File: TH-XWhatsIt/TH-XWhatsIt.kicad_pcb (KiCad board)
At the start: 2 copper layers, 162.2 x 18.8 mm, 25 parts, among them J1 BEAMSPRING CONNECTOR, J3 EXPANSION HEADER, U1 MCP4921-EP, U2 LM339, U3 74HCT595, U4 74HCT595, U5 ProMicro, U7 74HCT595

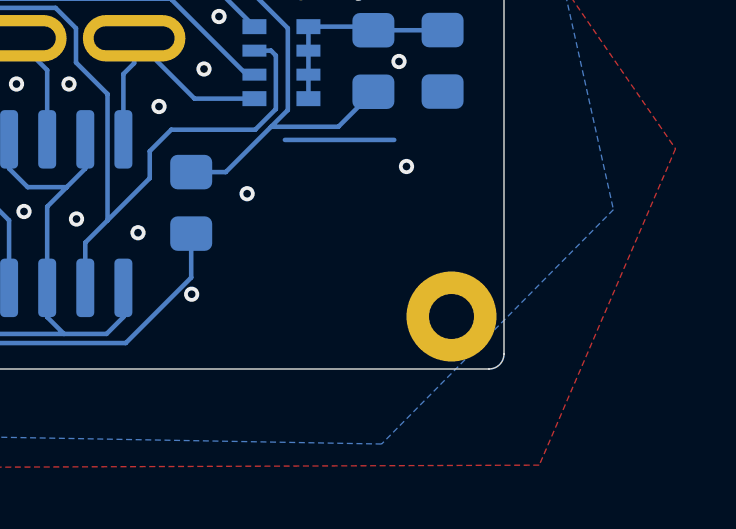
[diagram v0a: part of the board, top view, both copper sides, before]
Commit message: moved chassis gnd connection a little in order to get 3 connections to gnd plane
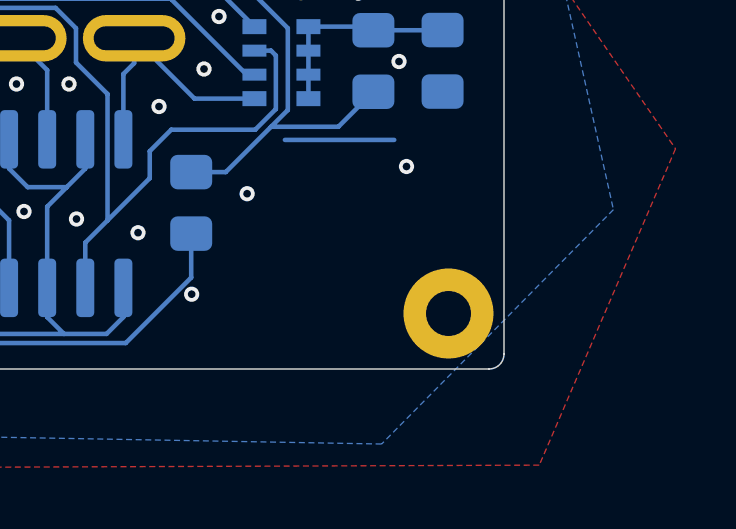
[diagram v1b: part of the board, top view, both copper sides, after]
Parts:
- moved H1 0.14 mm to (253.9, 158.9)
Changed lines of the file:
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@@
     (mod_text_size 1 1)
     (mod_text_width 0.15)
-    (pad_size 0.6 0.6)
-    (pad_drill 0.3)
+    (pad_size 3 3)
+    (pad_drill 1.5)
     (pad_to_mask_clearance 0.0508)
     (solder_mask_min_width 0.101)
@@
   )
   (module TH-XWhatsIt:ChassisGnd (layer B.Cu)
-    (at 254 159)
+    (at 253.9 158.9)
     (descr "Mounting Hole 2.2mm, M2")
     (tags "mounting hole 2.2mm m2")
@@
       (effects (font (size 1 1) (thickness 0.15)) (justify mirror))
     )
+    (fp_line (start -0.55 0.55) (end 2.95 0.55) (layer B.CrtYd) (width 0.05))
+    (fp_line (start 2.95 0.55) (end 2.95 -0.55) (layer B.CrtYd) (width 0.05))
+    (fp_line (start 2.95 -0.55) (end -0.55 -0.55) (layer B.CrtYd) (width 0.05))
+    (fp_line (start -0.55 -0.55) (end -0.55 0.55) (layer B.CrtYd) (width 0.05))
+    (fp_poly (pts (xy 0 0.3) (xy 2.4 0.3) (xy 2.4 -0.3) (xy 0 -0.3)) (layer F.Cu) (width 0))
     (fp_poly (pts (xy 0 0.3) (xy 2.4 0.3) (xy 2.4 -0.3) (xy 0 -0.3)) (layer B.Cu) (width 0))
-    (fp_poly (pts (xy 0 0.3) (xy 2.4 0.3) (xy 2.4 -0.3) (xy 0 -0.3)) (layer F.Cu) (width 0))
-    (fp_line (start -0.55 -0.55) (end -0.55 0.55) (layer B.CrtYd) (width 0.05))
-    (fp_line (start 2.95 -0.55) (end -0.55 -0.55) (layer B.CrtYd) (width 0.05))
-    (fp_line (start 2.95 0.55) (end 2.95 -0.55) (layer B.CrtYd) (width 0.05))
-    (fp_line (start -0.55 0.55) (end 2.95 0.55) (layer B.CrtYd) (width 0.05))
+    (pad 1 thru_hole circle (at 0 0) (size 0.6 0.6) (drill 0.3) (layers *.Cu)
+      (net 56 GNDD))
+    (pad 2 thru_hole circle (at 1.2 0) (size 0.6 0.6) (drill 0.3) (layers *.Cu)
+      (net 57 "Net-(NT1-Pad2)"))
     (pad 3 thru_hole circle (at 2.4 0) (size 0.6 0.6) (drill 0.3) (layers *.Cu)
       (net 44 GNDA) (zone_connect 2))
-    (pad 2 thru_hole circle (at 1.2 0) (size 0.6 0.6) (drill 0.3) (layers *.Cu)
-      (net 57 "Net-(NT1-Pad2)"))
-    (pad 1 thru_hole circle (at 0 0) (size 0.6 0.6) (drill 0.3) (layers *.Cu)
-      (net 56 GNDD))
   )
   (module Resistor_SMD:R_0805_2012Metric_Pad1.15x1.40mm_HandSolder (layer B.Cu)

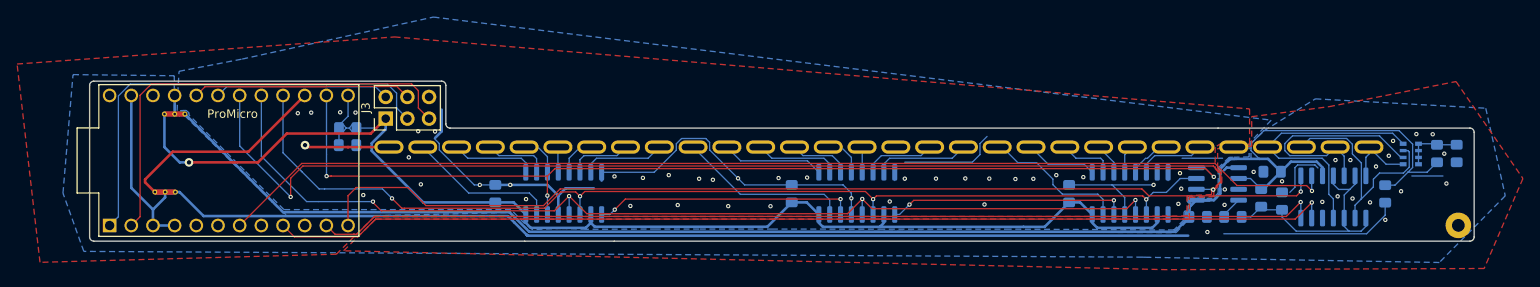
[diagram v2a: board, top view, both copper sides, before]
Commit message: more tweaks: corners bigger radius, some more rework on traces, and copper fills
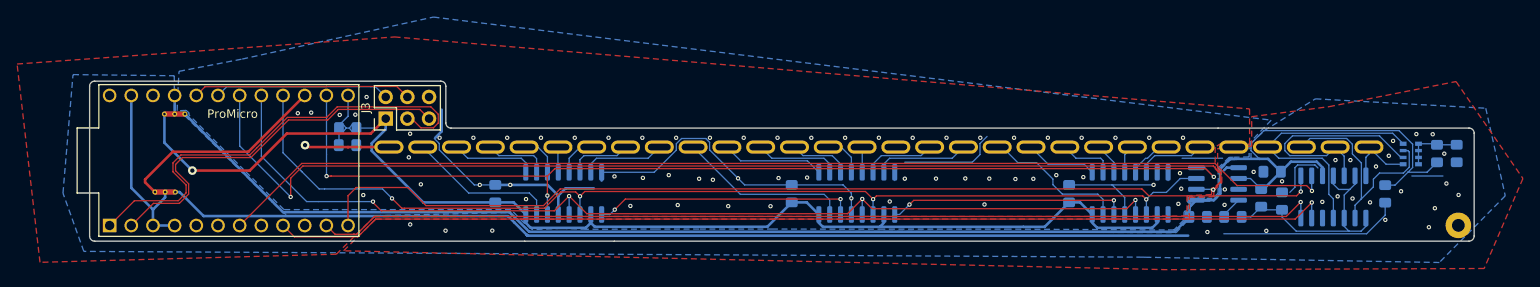
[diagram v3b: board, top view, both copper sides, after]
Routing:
- net HEADER2: track 53.3 -> 45.2 mm
- net HEADER1: track 52.7 -> 54.2 mm
- net GNDD: vias 40 -> 63
- net GNDA: vias 20 -> 27
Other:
- outline, holes or cut-outs redrawn

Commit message: single pcb: added tooling holes, position is only good for when pcbs are panelized back-to-back
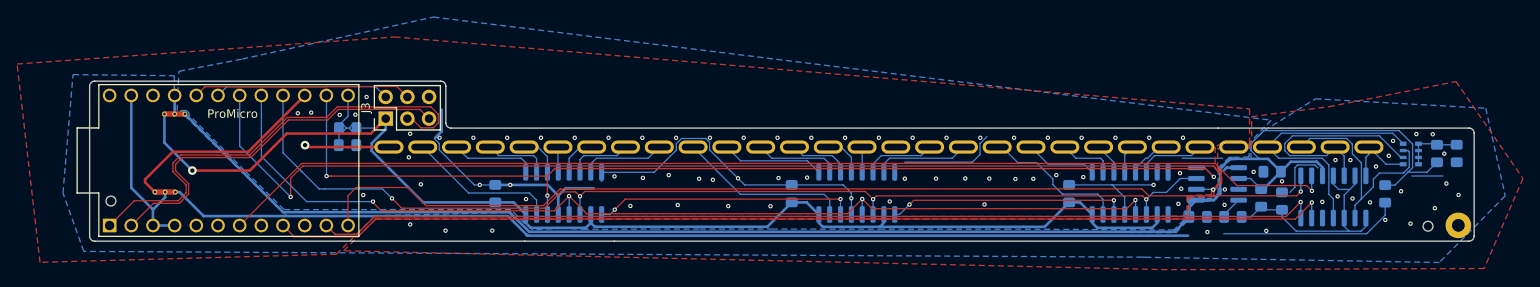
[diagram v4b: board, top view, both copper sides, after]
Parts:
- added REF**: tooling_hole, TH-XWhatsIt:tooling_hole, F.Cu at (96.0, 156.1)
- added REF**: tooling_hole, TH-XWhatsIt:tooling_hole, F.Cu at (250.3, 159.0)
